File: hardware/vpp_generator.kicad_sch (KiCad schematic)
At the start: 16 parts, among them Q5 TIP120, Q6 BC327, U2 74LS06N

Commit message: Rev.E. Updated specifications document and hardware design.
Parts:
- C8: footprint Capacitor_THT:C_Disc_D6.0mm_W2.5mm_P5.00mm -> (none)
- L2: footprint Inductor_THT:L_Toroid_Vertical_L16.0mm_W8.0mm_P7.62mm -> (none)
- Q6: value BC327 -> (none); footprint Package_TO_SOT_THT:TO-92_Inline_Wide -> (none)
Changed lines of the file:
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@@
       (effects (font (size 1.27 1.27)) (justify left))
     )
-    (property "Value" "BC327" (id 1) (at 119.1514 79.883 0)
-      (effects (font (size 1.27 1.27)) (justify left))
-    )
-    (property "Footprint" "Package_TO_SOT_THT:TO-92_Inline_Wide" (id 2) (at 119.38 76.835 0)
+    (property "Value" "" (id 1) (at 119.1514 79.883 0)
+      (effects (font (size 1.27 1.27)) (justify left))
+    )
+    (property "Footprint" "" (id 2) (at 119.38 76.835 0)
       (effects (font (size 1.27 1.27) italic) (justify left) hide)
     )
@@
       (effects (font (size 1.27 1.27)) (justify left))
     )
-    (property "Footprint" "Capacitor_THT:C_Disc_D6.0mm_W2.5mm_P5.00mm" (id 2) (at 117.8052 46.99 0)
+    (property "Footprint" "" (id 2) (at 117.8052 46.99 0)
       (effects (font (size 1.27 1.27)) hide)
     )
@@
       (effects (font (size 1.27 1.27)) (justify left))
     )
-    (property "Footprint" "Inductor_THT:L_Toroid_Vertical_L16.0mm_W8.0mm_P7.62mm" (id 2) (at 101.6 30.48 0)
-      (effects (font (size 1.27 1.27)) hide)
-    )
+    (property "Footprint" "" (id 2) (at 101.6 30.48 0)
+      (effects (font (size 1.27 1.27)) hide)
+    )

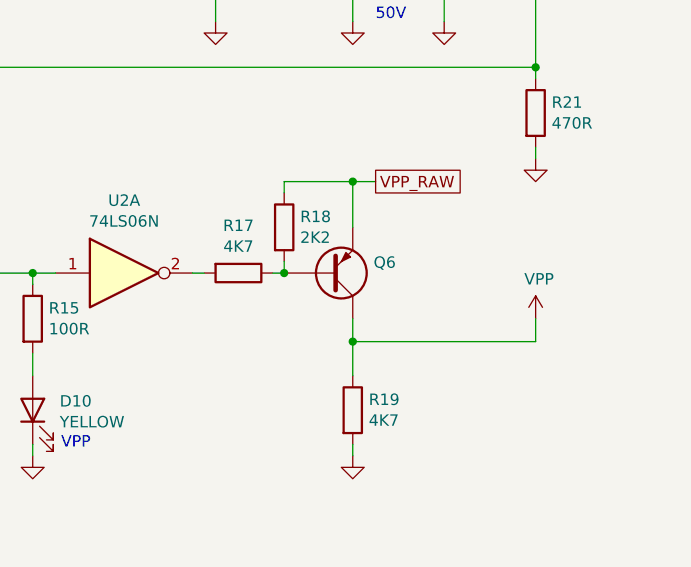
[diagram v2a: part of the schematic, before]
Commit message: Rev.E. Updated R51 wattage.
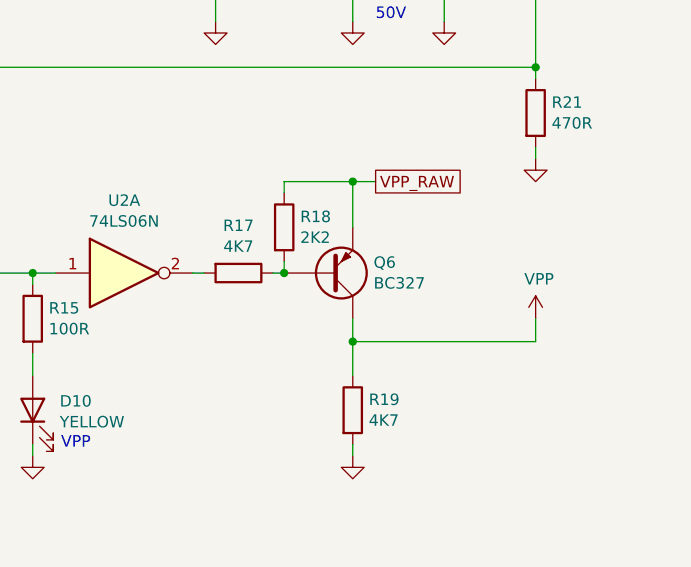
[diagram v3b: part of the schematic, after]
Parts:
- C8: footprint (none) -> Capacitor_THT:CP_Radial_D8.0mm_P3.50mm
- L2: footprint (none) -> Inductor_THT:L_Toroid_Vertical_L13.0mm_W6.5mm_P5.60mm
- Q6: value (none) -> BC327; footprint (none) -> Package_TO_SOT_THT:TO-92_Inline_Wide
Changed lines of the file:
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@@
       (effects (font (size 1.27 1.27)) (justify left))
     )
-    (property "Value" "" (id 1) (at 119.1514 79.883 0)
-      (effects (font (size 1.27 1.27)) (justify left))
-    )
-    (property "Footprint" "" (id 2) (at 119.38 76.835 0)
+    (property "Value" "BC327" (id 1) (at 119.1514 79.883 0)
+      (effects (font (size 1.27 1.27)) (justify left))
+    )
+    (property "Footprint" "Package_TO_SOT_THT:TO-92_Inline_Wide" (id 2) (at 119.38 76.835 0)
       (effects (font (size 1.27 1.27) italic) (justify left) hide)
     )
@@
       (effects (font (size 1.27 1.27)) (justify left))
     )
-    (property "Footprint" "" (id 2) (at 117.8052 46.99 0)
+    (property "Footprint" "Capacitor_THT:CP_Radial_D8.0mm_P3.50mm" (id 2) (at 117.8052 46.99 0)
       (effects (font (size 1.27 1.27)) hide)
     )
@@
       (effects (font (size 1.27 1.27)) (justify left))
     )
-    (property "Footprint" "" (id 2) (at 101.6 30.48 0)
-      (effects (font (size 1.27 1.27)) hide)
-    )
+    (property "Footprint" "Inductor_THT:L_Toroid_Vertical_L13.0mm_W6.5mm_P5.60mm" (id 2) (at 101.6 30.48 0)
+      (effects (font (size 1.27 1.27)) hide)
+    )

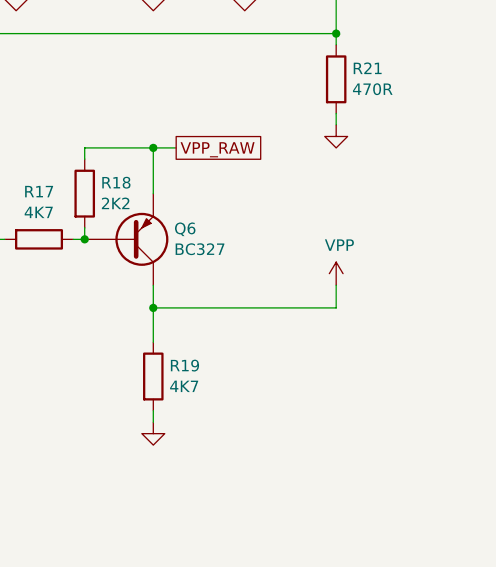
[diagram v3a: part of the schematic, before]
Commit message: Rev.E. Add Test Points for VDD/VPP/GND.
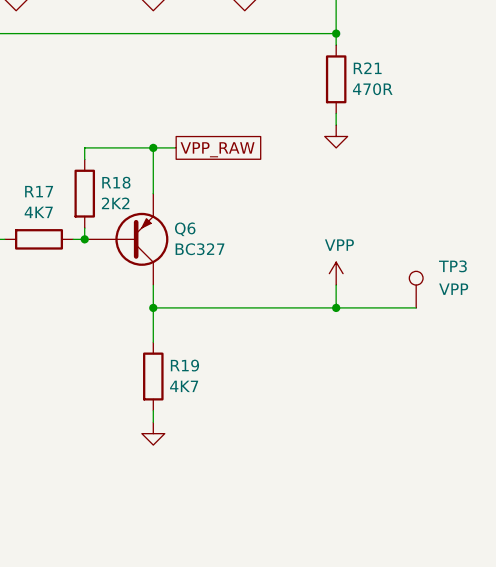
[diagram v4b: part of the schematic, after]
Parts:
- added TP3: VPP, TestPoint:TestPoint_THTPad_2.5x2.5mm_Drill1.2mm, symbol Connector:TestPoint
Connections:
- net VPP: now also TP3.1
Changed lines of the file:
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@@
   (junction (at 137.16 55.88) (diameter 0) (color 0 0 0 0)
   )
+  (junction (at 137.16 86.36) (diameter 0) (color 0 0 0 0)
+  )
   (junction (at 137.16 38.1) (diameter 0) (color 0 0 0 0)
   )
@@
   )
   (junction (at 101.6 38.1) (diameter 0) (color 0 0 0 0)
+  )
+  (wire (pts (xy 137.16 86.36) (xy 146.05 86.36))
+    (stroke (width 0) (type default) (color 0 0 0 0))
   )
   (wire (pts (xy 71.12 43.18) (xy 82.55 43.18))
@@
     (pin "1")
     (pin "2")
-    (pin "3")
-    (pin "4")
-    (pin "5")
-    (pin "6")
-    (pin "8")
-    (pin "9")
-    (pin "10")
-    (pin "11")
-    (pin "12")
-    (pin "13")
-    (pin "14")
-    (pin "7")
   )
   (symbol (lib_id "74xx:74LS06N") (at 33.02 111.76 0) (unit 7)
@@
       (effects (font (size 1.27 1.27)) hide)
     )
-    (pin "1")
-    (pin "2")
-    (pin "3")
-    (pin "4")
-    (pin "5")
-    (pin "6")
-    (pin "8")
-    (pin "9")
-    (pin "10")
-    (pin "11")
-    (pin "12")
-    (pin "13")
     (pin "14")
     (pin "7")
@@
       (effects (font (size 1.27 1.27)) hide)
     )
+    (pin "1")
+  )
+  (symbol (lib_id "Connector:TestPoint") (at 146.05 86.36 0) (unit 1)
+    (in_bom yes) (on_board yes) (fields_autoplaced)
+    (property "Reference" "TP3" (id 0) (at 148.59 81.7879 0)
+      (effects (font (size 1.27 1.27)) (justify left))
+    )
+    (property "Value" "VPP" (id 1) (at 148.59 84.3279 0)
+      (effects (font (size 1.27 1.27)) (justify left))
+    )
+    (property "Footprint" "TestPoint:TestPoint_THTPad_2.5x2.5mm_Drill1.2mm" (id 2) (at 151.13 86.36 0)
+      (effects (font (size 1.27 1.27)) hide)
+    )
+    (property "Datasheet" "~" (id 3) (at 151.13 86.36 0)
+      (effects (font (size 1.27 1.27)) hide)
+    )
